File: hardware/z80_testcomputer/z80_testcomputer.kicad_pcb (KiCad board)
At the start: 2 copper layers, 95 x 100 mm, 13 parts, among them J1 Conn_02x15_Odd_Even, J2 Conn_02x15_Odd_Even, U1 Z84C000XPEG

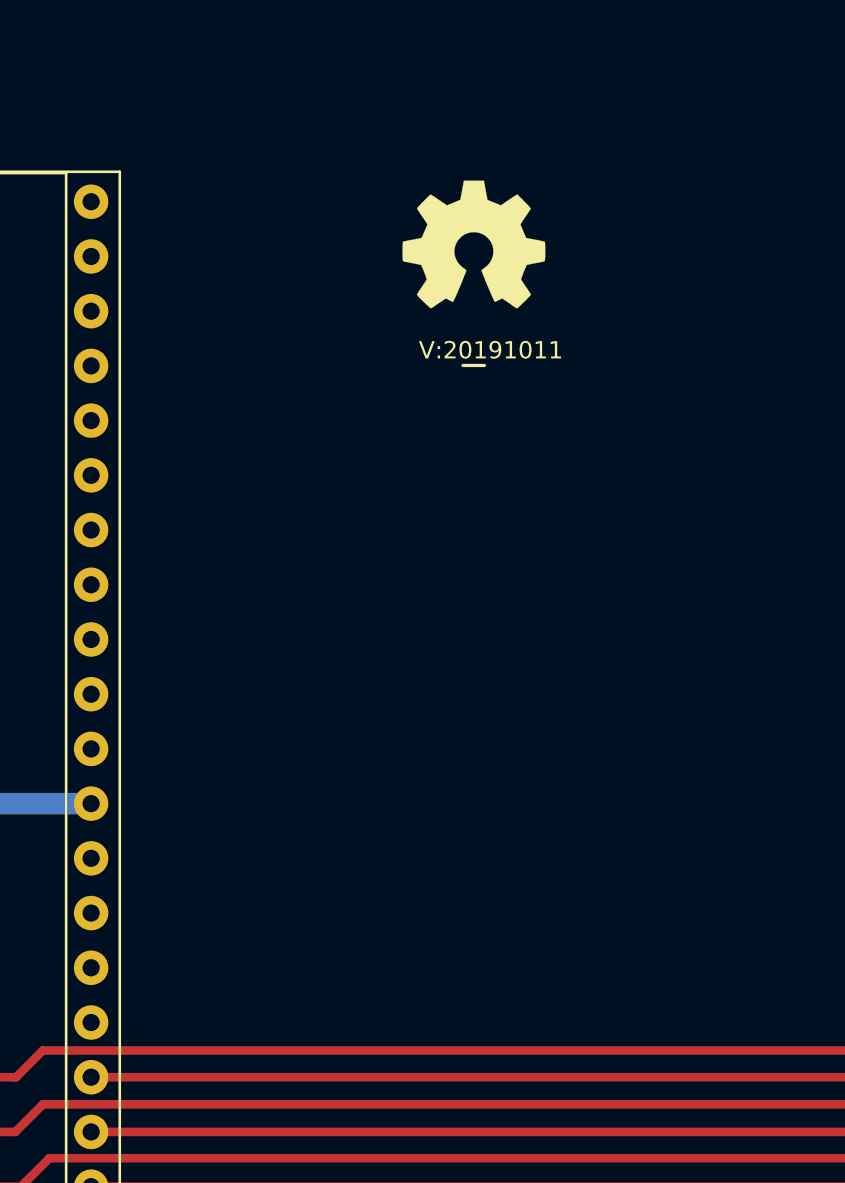
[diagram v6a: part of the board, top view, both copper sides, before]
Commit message: experimenting with SRAM placement, PDIP is too big, need to switch to PLCC memories/processor
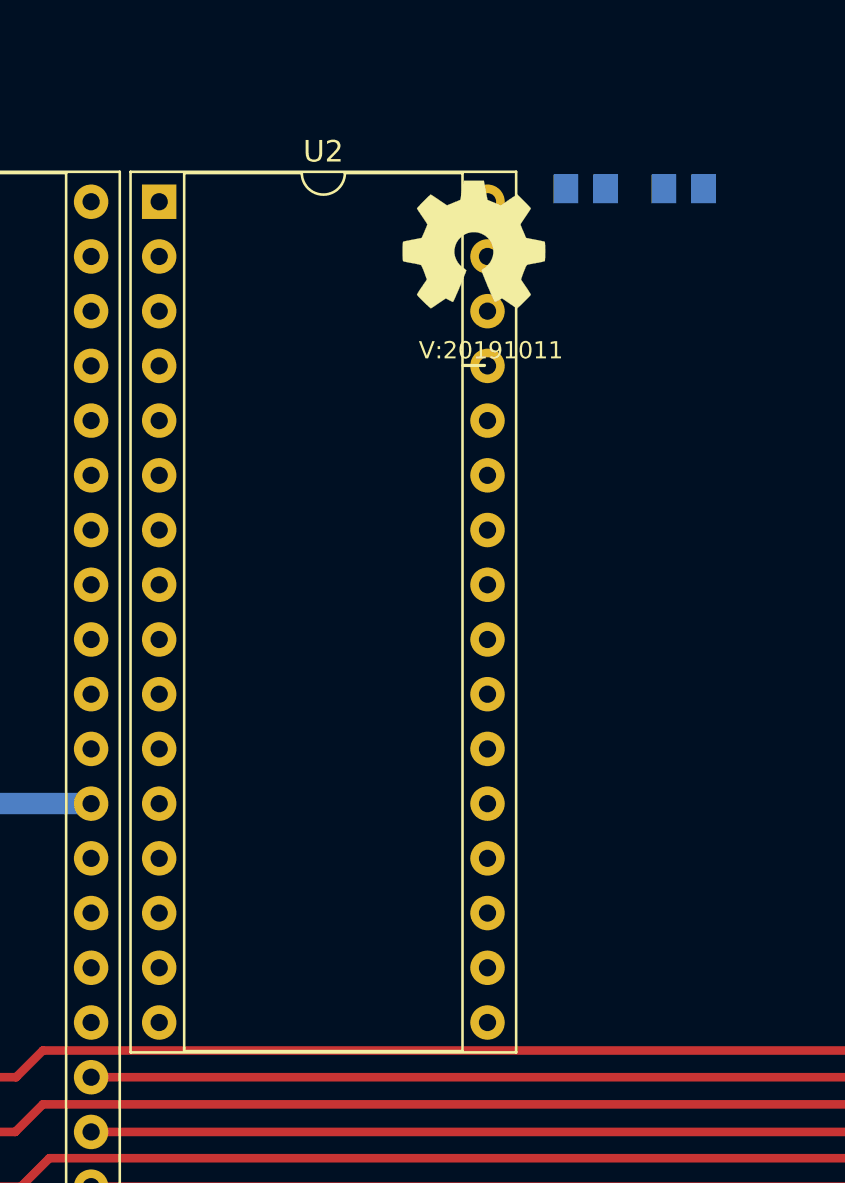
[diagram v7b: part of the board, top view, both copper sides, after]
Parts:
- added C3: 100n, SquantorRcl:C_0805+0603, B.Cu at (155.2, 97.4)
- added C4: 1u, SquantorRcl:C_0805+0603, B.Cu at (159.8, 97.4)
- added U2: SRAM_512K8B_DIP_SOP_SOJ, Package_DIP:DIP-32_W15.24mm_Socket, F.Cu at (135.4, 98.0)
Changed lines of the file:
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@@
     (tracks 77)
     (zones 0)
-    (modules 13)
+    (modules 16)
     (nets 41)
   )
@@
   )
   (setup
-    (last_trace_width 0.4)
+    (last_trace_width 0.127)
     (user_trace_width 0.15)
     (user_trace_width 0.2)
@@
     (add_net /A14)
     (add_net /A15)
+    (add_net /A16)
+    (add_net /A17)
+    (add_net /A18)
     (add_net /A2)
     (add_net /A3)
@@
     (add_net "Net-(J1-Pad8)")
     (add_net "Net-(J1-Pad9)")
+    (add_net "Net-(U2-Pad22)")
+    (add_net "Net-(U2-Pad24)")
+    (add_net "Net-(U2-Pad29)")
+  )
+  (module Package_DIP:DIP-32_W15.24mm_Socket (layer F.Cu)
+    (at 135.4 98)
+    (descr "32-lead though-hole mounted DIP package, row spacing 15.24 mm (600 mils), Socket")
+    (tags "THT DIP DIL PDIP 2.54mm 15.24mm 600mil Socket")
+    (fp_text reference U2 (at 7.62 -2.33) (layer F.SilkS)
+      (effects (font (size 1 1) (thickness 0.15)))
+    )
+    (fp_text value SRAM_512K8B_DIP_SOP_SOJ (at 7.62 40.43) (layer F.Fab)
+      (effects (font (size 1 1) (thickness 0.15)))
+    )
+    (fp_text user %R (at 7.62 19.05) (layer F.Fab)
+      (effects (font (size 1 1) (thickness 0.15)))
+    )
+    (fp_line (start 16.8 -1.6) (end -1.55 -1.6) (layer F.CrtYd) (width 0.05))
+    (fp_line (start 16.8 39.7) (end 16.8 -1.6) (layer F.CrtYd) (width 0.05))
+    (fp_line (start -1.55 39.7) (end 16.8 39.7) (layer F.CrtYd) (width 0.05))
+    (fp_line (start -1.55 -1.6) (end -1.55 39.7) (layer F.CrtYd) (width 0.05))
+    (fp_line (start 16.57 -1.39) (end -1.33 -1.39) (layer F.SilkS) (width 0.12))
+    (fp_line (start 16.57 39.49) (end 16.57 -1.39) (layer F.SilkS) (width 0.12))
+    (fp_line (start -1.33 39.49) (end 16.57 39.49) (layer F.SilkS) (width 0.12))
+    (fp_line (start -1.33 -1.39) (end -1.33 39.49) (layer F.SilkS) (width 0.12))
+    (fp_line (start 14.08 -1.33) (end 8.62 -1.33) (layer F.SilkS) (width 0.12))
+    (fp_line (start 14.08 39.43) (end 14.08 -1.33) (layer F.SilkS) (width 0.12))
+    (fp_line (start 1.16 39.43) (end 14.08 39.43) (layer F.SilkS) (width 0.12))
+    (fp_line (start 1.16 -1.33) (end 1.16 39.43) (layer F.SilkS) (width 0.12))
+    (fp_line (start 6.62 -1.33) (end 1.16 -1.33) (layer F.SilkS) (width 0.12))
+    (fp_line (start 16.51 -1.33) (end -1.27 -1.33) (layer F.Fab) (width 0.1))
+    (fp_line (start 16.51 39.43) (end 16.51 -1.33) (layer F.Fab) (width 0.1))
+    (fp_line (start -1.27 39.43) (end 16.51 39.43) (layer F.Fab) (width 0.1))
+    (fp_line (start -1.27 -1.33) (end -1.27 39.43) (layer F.Fab) (width 0.1))
+    (fp_line (start 0.255 -0.27) (end 1.255 -1.27) (layer F.Fab) (width 0.1))
+    (fp_line (start 0.255 39.37) (end 0.255 -0.27) (layer F.Fab) (width 0.1))
+    (fp_line (start 14.985 39.37) (end 0.255 39.37) (layer F.Fab) (width 0.1))
+    (fp_line (start 14.985 -1.27) (end 14.985 39.37) (layer F.Fab) (width 0.1))
+    (fp_line (start 1.255 -1.27) (end 14.985 -1.27) (layer F.Fab) (width 0.1))
+    (fp_arc (start 7.62 -1.33) (end 6.62 -1.33) (angle -180) (layer F.SilkS) (width 0.12))
+    (pad 32 thru_hole oval (at 15.24 0) (size 1.6 1.6) (drill 0.8) (layers *.Cu *.Mask)
+      (net 2 /VDD))
+    (pad 16 thru_hole oval (at 0 38.1) (size 1.6 1.6) (drill 0.8) (layers *.Cu *.Mask)
+      (net 1 /VSS))
+    (pad 31 thru_hole oval (at 15.24 2.54) (size 1.6 1.6) (drill 0.8) (layers *.Cu *.Mask)
+      (net 32 /A15))
+    (pad 15 thru_hole oval (at 0 35.56) (size 1.6 1.6) (drill 0.8) (layers *.Cu *.Mask)
+      (net 20 /D2))
+    (pad 30 thru_hole oval (at 15.24 5.08) (size 1.6 1.6) (drill 0.8) (layers *.Cu *.Mask))
+    (pad 14 thru_hole oval (at 0 33.02) (size 1.6 1.6) (drill 0.8) (layers *.Cu *.Mask)
+      (net 14 /D1))
+    (pad 29 thru_hole oval (at 15.24 7.62) (size 1.6 1.6) (drill 0.8) (layers *.Cu *.Mask))
+    (pad 13 thru_hole oval (at 0 30.48) (size 1.6 1.6) (drill 0.8) (layers *.Cu *.Mask)
+      (net 16 /D0))
+    (pad 28 thru_hole oval (at 15.24 10.16) (size 1.6 1.6) (drill 0.8) (layers *.Cu *.Mask)
+      (net 36 /A13))
+    (pad 12 thru_hole oval (at 0 27.94) (size 1.6 1.6) (drill 0.8) (layers *.Cu *.Mask)
+      (net 22 /A0))
+    (pad 27 thru_hole oval (at 15.24 12.7) (size 1.6 1.6) (drill 0.8) (layers *.Cu *.Mask)
+      (net 7 /A8))
+    (pad 11 thru_hole oval (at 0 25.4) (size 1.6 1.6) (drill 0.8) (layers *.Cu *.Mask)
+      (net 21 /A1))
+    (pad 26 thru_hole oval (at 15.24 15.24) (size 1.6 1.6) (drill 0.8) (layers *.Cu *.Mask)
+      (net 5 /A9))
+    (pad 10 thru_hole oval (at 0 22.86) (size 1.6 1.6) (drill 0.8) (layers *.Cu *.Mask)
+      (net 19 /A2))
+    (pad 25 thru_hole oval (at 15.24 17.78) (size 1.6 1.6) (drill 0.8) (layers *.Cu *.Mask)
+      (net 40 /A11))
+    (pad 9 thru_hole oval (at 0 20.32) (size 1.6 1.6) (drill 0.8) (layers *.Cu *.Mask)
+      (net 17 /A3))
+    (pad 24 thru_hole oval (at 15.24 20.32) (size 1.6 1.6) (drill 0.8) (layers *.Cu *.Mask))
+    (pad 8 thru_hole oval (at 0 17.78) (size 1.6 1.6) (drill 0.8) (layers *.Cu *.Mask)
+      (net 15 /A4))
+    (pad 23 thru_hole oval (at 15.24 22.86) (size 1.6 1.6) (drill 0.8) (layers *.Cu *.Mask)
+      (net 3 /A10))
+    (pad 7 thru_hole oval (at 0 15.24) (size 1.6 1.6) (drill 0.8) (layers *.Cu *.Mask)
+      (net 13 /A5))
+    (pad 22 thru_hole oval (at 15.24 25.4) (size 1.6 1.6) (drill 0.8) (layers *.Cu *.Mask))
+    (pad 6 thru_hole oval (at 0 12.7) (size 1.6 1.6) (drill 0.8) (layers *.Cu *.Mask)
+      (net 11 /A6))
+    (pad 21 thru_hole oval (at 15.24 27.94) (size 1.6 1.6) (drill 0.8) (layers *.Cu *.Mask)
+      (net 18 /D7))
+    (pad 5 thru_hole oval (at 0 10.16) (size 1.6 1.6) (drill 0.8) (layers *.Cu *.Mask)
+      (net 9 /A7))
+    (pad 20 thru_hole oval (at 15.24 30.48) (size 1.6 1.6) (drill 0.8) (layers *.Cu *.Mask)
+      (net 23 /D6))
+    (pad 4 thru_hole oval (at 0 7.62) (size 1.6 1.6) (drill 0.8) (layers *.Cu *.Mask)
+      (net 38 /A12))
+    (pad 19 thru_hole oval (at 15.24 33.02) (size 1.6 1.6) (drill 0.8) (layers *.Cu *.Mask)
+      (net 24 /D5))
+    (pad 3 thru_hole oval (at 0 5.08) (size 1.6 1.6) (drill 0.8) (layers *.Cu *.Mask)
+      (net 34 /A14))
+    (pad 18 thru_hole oval (at 15.24 35.56) (size 1.6 1.6) (drill 0.8) (layers *.Cu *.Mask)
+      (net 28 /D4))
+    (pad 2 thru_hole oval (at 0 2.54) (size 1.6 1.6) (drill 0.8) (layers *.Cu *.Mask))
+    (pad 17 thru_hole oval (at 15.24 38.1) (size 1.6 1.6) (drill 0.8) (layers *.Cu *.Mask)
+      (net 26 /D3))
+    (pad 1 thru_hole rect (at 0 0) (size 1.6 1.6) (drill 0.8) (layers *.Cu *.Mask))
+    (model ${KISYS3DMOD}/Package_DIP.3dshapes/DIP-32_W15.24mm_Socket.wrl
+      (at (xyz 0 0 0))
+      (scale (xyz 1 1 1))
+      (rotate (xyz 0 0 0))
+    )
   )
   (module SquantorRcl:C_0805+0603 (layer B.Cu)
+    (at 159.75 97.4)
+    (descr "Capacitor SMD 0805 and 0603 pad sizes, reflow soldering, based on AVX dimensions")
+    (tags "capacitor 0805 0603 mixed")
+    (attr smd)
+    (fp_text reference C4 (at 0 2.1) (layer B.SilkS)
+      (effects (font (size 1 1) (thickness 0.15)) (justify mirror))
+    )
+    (fp_text value 1u (at 0 -2.1) (layer B.Fab)
+      (effects (font (size 1 1) (thickness 0.15)) (justify mirror))
+    )
+    (fp_line (start 0 0.6) (end 0 -0.6) (layer B.SilkS) (width 0.15))
+    (fp_line (start -0.9 -0.625) (end -0.9 0.625) (layer B.Fab) (width 0.1))
+    (fp_line (start 0.9 -0.625) (end -0.9 -0.625) (layer B.Fab) (width 0.1))
+    (fp_line (start 0.9 0.625) (end 0.9 -0.625) (layer B.Fab) (width 0.1))
+    (fp_line (start -0.9 0.625) (end 0.9 0.625) (layer B.Fab) (width 0.1))
+    (fp_line (start -1.75 0.95) (end 1.75 0.95) (layer B.CrtYd) (width 0.05))
+    (fp_line (start -1.75 -0.95) (end 1.75 -0.95) (layer B.CrtYd) (width 0.05))
+    (fp_line (start -1.75 0.95) (end -1.75 -0.95) (layer B.CrtYd) (width 0.05))
+    (fp_line (start 1.75 0.95) (end 1.75 -0.95) (layer B.CrtYd) (width 0.05))
+    (pad 1 smd rect (at -0.925 0) (size 1.15 1.35) (layers B.Cu B.Paste B.Mask)
+      (net 1 /VSS))
+    (pad 2 smd rect (at 0.925 0) (size 1.15 1.35) (layers B.Cu B.Paste B.Mask)
+      (net 2 /VDD))
+    (model ${KISYS3DMOD}/Capacitor_SMD.3dshapes/C_0805_2012Metric.step
+      (at (xyz 0 0 0))
+      (scale (xyz 1 1 1))
+      (rotate (xyz 0 0 0))
+    )
+  )
+  (module SquantorRcl:C_0805+0603 (layer B.Cu)
+    (at 155.2 97.4)
+    (descr "Capacitor SMD 0805 and 0603 pad sizes, reflow soldering, based on AVX dimensions")
+    (tags "capacitor 0805 0603 mixed")
+    (attr smd)
+    (fp_text reference C3 (at 0 2.1) (layer B.SilkS)
+      (effects (font (size 1 1) (thickness 0.15)) (justify mirror))
+    )
+    (fp_text value 100n (at 0 -2.1) (layer B.Fab)
+      (effects (font (size 1 1) (thickness 0.15)) (justify mirror))
+    )
+    (fp_line (start 0 0.6) (end 0 -0.6) (layer B.SilkS) (width 0.15))
+    (fp_line (start -0.9 -0.625) (end -0.9 0.625) (layer B.Fab) (width 0.1))
+    (fp_line (start 0.9 -0.625) (end -0.9 -0.625) (layer B.Fab) (width 0.1))
+    (fp_line (start 0.9 0.625) (end 0.9 -0.625) (layer B.Fab) (width 0.1))
+    (fp_line (start -0.9 0.625) (end 0.9 0.625) (layer B.Fab) (width 0.1))
+    (fp_line (start -1.75 0.95) (end 1.75 0.95) (layer B.CrtYd) (width 0.05))
+    (fp_line (start -1.75 -0.95) (end 1.75 -0.95) (layer B.CrtYd) (width 0.05))
+    (fp_line (start -1.75 0.95) (end -1.75 -0.95) (layer B.CrtYd) (width 0.05))
+    (fp_line (start 1.75 0.95) (end 1.75 -0.95) (layer B.CrtYd) (width 0.05))
+    (pad 1 smd rect (at -0.925 0) (size 1.15 1.35) (layers B.Cu B.Paste B.Mask)
+      (net 1 /VSS))
+    (pad 2 smd rect (at 0.925 0) (size 1.15 1.35) (layers B.Cu B.Paste B.Mask)
+      (net 2 /VDD))
+    (model ${KISYS3DMOD}/Capacitor_SMD.3dshapes/C_0805_2012Metric.step
+      (at (xyz 0 0 0))
+      (scale (xyz 1 1 1))
+      (rotate (xyz 0 0 0))
+    )
+  )
+  (module SquantorRcl:C_0805+0603 (layer B.Cu)

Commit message: additional package changes
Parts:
- U1: value Z84C000XPEG -> Z84C000XVEG; footprint Package_DIP:DIP-40_W15.24mm_Socket -> Package_LCC:PLCC-44_SMD-Socket
- U2: footprint Package_DIP:DIP-32_W15.24mm_Socket -> Package_SO:SSOP-32_11.305x20.495mm_P1.27mm
- moved U2 31.9 mm to (148.7, 127.0), turned to 90 degrees
- moved C4 31.7 mm to (149.1, 127.3), turned to 90 degrees
- moved C3 31.0 mm to (147.1, 127.3), turned to 90 degrees
- moved U1 18.9 mm to (123.4, 115.8)
- moved C1 8.37 mm to (123.4, 117.5)
- moved C2 8.37 mm to (123.4, 115.5)
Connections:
- U1 pad 10: /D6 -> /D5
- U1 pad 11: /VDD -> /D6
- U1 pad 12: /D2 -> (no net)
- U1 pad 13: /D7 -> /VDD
- U1 pad 14: /D0 -> /D2
- U1 pad 15: /D1 -> /D7
- U1 pad 16: /!INT -> /D0
- U1 pad 17: /!NMI -> /D1
- U1 pad 18: /!HALT -> /!INT
- U1 pad 19: /!MREQ -> /!NMI
- U1 pad 20: /!IORQ -> /!HALT
- U1 pad 21: /!RD -> /!MREQ
- U1 pad 22: /!WR -> /!IORQ
- U1 pad 23: /!BUSACK -> /!RD
- U1 pad 24: /!WAIT -> (no net)
- U1 pad 25: /!BUSREQ -> (no net)
- U1 pad 26: /!RESET -> /!WR
- U1 pad 27: /!M1 -> /!BUSACK
- U1 pad 28: /!RFSH -> /!WAIT
- U1 pad 29: /VSS -> /!BUSREQ
- U1 pad 30: /A0 -> /!RESET
- U1 pad 31: /A1 -> /!M1
- U1 pad 32: /A2 -> /!RFSH
- U1 pad 33: /A3 -> /VSS
- U1 pad 34: /A4 -> /A0
- U1 pad 35: /A5 -> /A1
- U1 pad 36: /A6 -> /A2
- U1 pad 37: /A7 -> /A3
- U1 pad 38: /A8 -> /A4
- U1 pad 39: /A9 -> /A5
- U1 pad 40: /A10 -> /A6
- U1 pad 6: /MCLK -> (no net)
- U1 pad 7: /D4 -> /MCLK
- U1 pad 8: /D3 -> /D4
- U1 pad 9: /D5 -> /D3
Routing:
- net /VDD: track 143.2 -> 73.7 mm
- net /VSS: track 225.1 -> 157.5 mm
- net /!IORQ: track 75.5 -> 61.6 mm
- net /!MREQ: track 75.5 -> 61.6 mm
- net /!HALT: track 75.5 -> 61.9 mm
- net /!NMI: track 75.5 -> 62.0 mm
